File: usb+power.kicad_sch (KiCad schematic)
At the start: 43 parts, among them J1 USB_C_Receptacle_USB2.0_16P, U1 SRV05-4

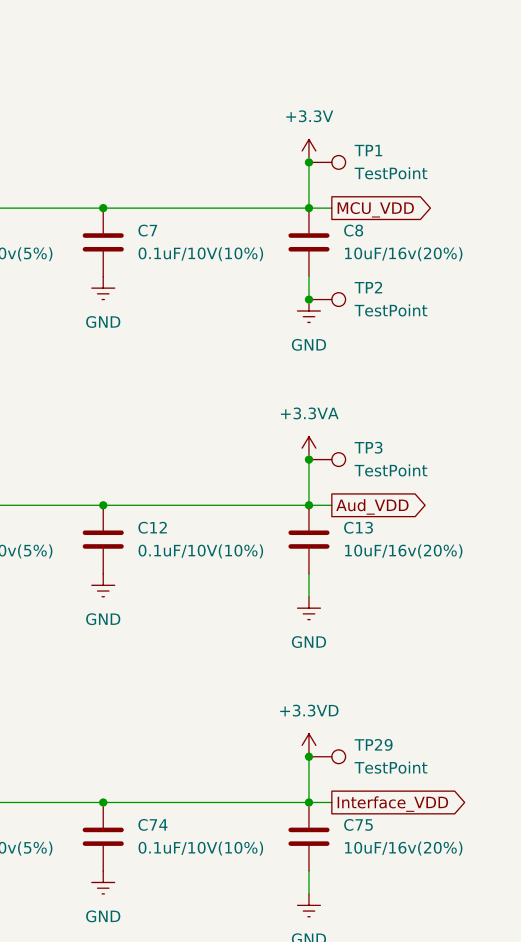
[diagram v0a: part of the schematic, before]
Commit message: Initial population of PCB
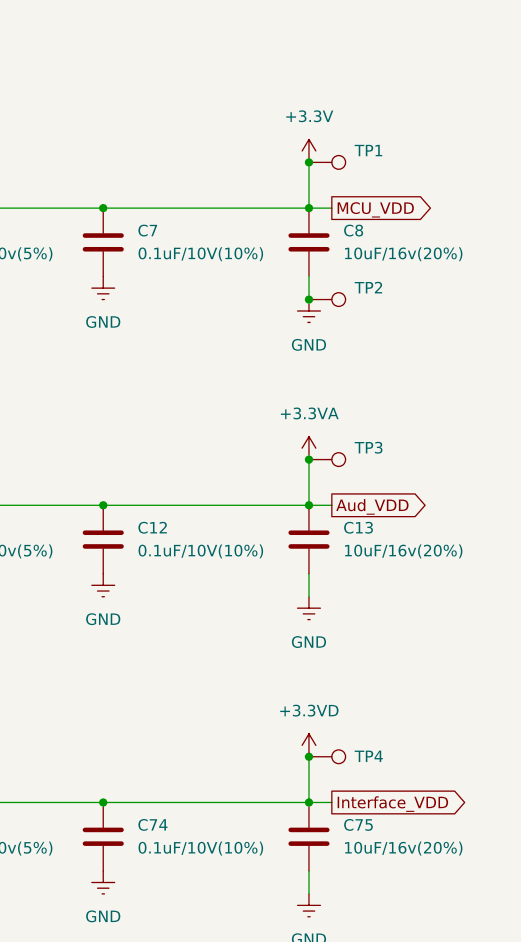
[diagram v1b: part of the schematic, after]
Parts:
- removed TP29: TestPoint, TestPoint:TestPoint_Pad_D1.5mm, symbol Connector:TestPoint
- added TP4: TestPoint, TestPoint:TestPoint_Pad_D1.5mm, symbol Connector:TestPoint
- TP2: footprint (none) -> TestPoint:TestPoint_Pad_D1.5mm
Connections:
- net +3.3VD: now also TP4.1
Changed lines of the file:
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@@
 	)
 	(junction
+		(at 256.54 120.65)
+		(diameter 0)
+		(color 0 0 0 0)
+	)
+	(junction
 		(at 160.02 92.71)
 		(diameter 0)
@@
 	)
 	(junction
-		(at 114.3 125.73)
+		(at 256.54 69.85)
 		(diameter 0)
 		(color 0 0 0 0)
 	)
 	(junction
-		(at 256.54 69.85)
+		(at 114.3 125.73)
 		(diameter 0)
 		(color 0 0 0 0)
@@
 		(color 0 0 0 0)
 	)
-	(junction
-		(at 256.54 120.65)
-		(diameter 0)
-		(color 0 0 0 0)
-	)
 	(no_connect
 		(at 88.9 55.88)
@@
 	)
 	(symbol
-		(lib_id "Diode:SS24")
-		(at 102.87 27.94 180)
+		(lib_id "Connector:TestPoint")
+		(at 256.54 120.65 270)
 		(unit 1)
 		(exclude_from_sim no)
@@
 		(dnp no)
 		(fields_autoplaced yes)
-		(property "Reference" "D1"
-			(at 103.1875 21.59 0)
+		(property "Reference" "TP4"
+			(at 261.62 120.6499 90)
 			(effects
 				(font
 					(size 1.27 1.27)
 				)
+				(justify left)
 			)
 		)
-		(property "Value" "SS24"
-			(at 103.1875 24.13 0)
+		(property "Value" "TestPoint"
+			(at 261.1119 118.11 0)
 			(effects
 				(font
 					(size 1.27 1.27)
 				)
+				(justify right)
+				(hide yes)
 			)
 		)
-		(property "Footprint" "Diode_SMD:D_SMA"
-			(at 102.87 23.495 0)
+		(property "Footprint" "TestPoint:TestPoint_Pad_D1.5mm"
+			(at 256.54 125.73 0)
 			(effects
 				(font
@@
 			)
 		)
-		(property "Datasheet" "https://www.vishay.com/docs/88748/ss22.pdf"
-			(at 102.87 27.94 0)
+		(property "Datasheet" "~"
+			(at 256.54 125.73 0)
 			(effects
 				(font
@@
 			)
 		)
-		(property "Description" "40V 2A Schottky Diode, SMA"
-			(at 102.87 27.94 0)
+		(property "Description" "test point"
+			(at 256.54 120.65 0)
 			(effects
 				(font
@@
 		(pin "1"
 		)
-		(pin "2"
-		)
 		(instances
 			(project "Wave"
 				(path "/d9ae5ab6-a812-4d0b-96e5-05f704754669/5faeef98-962c-45cf-bbaf-2cc942880b89"
-					(reference "D1")
+					(reference "TP4")
 					(unit 1)
 				)
@@
 	)
 	(symbol
-		(lib_id "Connector:TestPoint")
-		(at 256.54 69.85 270)
+		(lib_id "Diode:SS24")
+		(at 102.87 27.94 180)
 		(unit 1)
 		(exclude_from_sim no)
@@
 		(dnp no)
 		(fields_autoplaced yes)
-		(property "Reference" "TP2"
-			(at 261.62 68.5799 90)
+		(property "Reference" "D1"
+			(at 103.1875 21.59 0)
 			(effects
 				(font
 					(size 1.27 1.27)
 				)
-				(justify left)
 			)
 		)
-		(property "Value" "TestPoint"
-			(at 261.62 71.1199 90)
+		(property "Value" "SS24"
+			(at 103.1875 24.13 0)
 			(effects
 				(font
 					(size 1.27 1.27)
 				)
-				(justify left)
 			)
 		)
-		(property "Footprint" ""
-			(at 256.54 74.93 0)
+		(property "Footprint" "Diode_SMD:D_SMA"
+			(at 102.87 23.495 0)
 			(effects
 				(font
@@
 			)
 		)
-		(property "Datasheet" "~"
-			(at 256.54 74.93 0)
+		(property "Datasheet" "https://www.vishay.com/docs/88748/ss22.pdf"
+			(at 102.87 27.94 0)
 			(effects
 				(font
@@
 			)
 		)
-		(property "Description" "test point"
-			(at 256.54 69.85 0)
+		(property "Description" "40V 2A Schottky Diode, SMA"
+			(at 102.87 27.94 0)
 			(effects
 				(font
@@
 		(pin "1"
 		)
+		(pin "2"
+		)
 		(instances
 			(project "Wave"
 				(path "/d9ae5ab6-a812-4d0b-96e5-05f704754669/5faeef98-962c-45cf-bbaf-2cc942880b89"
-					(reference "TP2")
+					(reference "D1")
 					(unit 1)
 				)
@@
 	)
 	(symbol
+		(lib_id "Connector:TestPoint")
+		(at 256.54 69.85 270)
+		(unit 1)
+		(exclude_from_sim no)
+		(in_bom yes)
+		(on_board yes)
+		(dnp no)
+		(fields_autoplaced yes)
+		(property "Reference" "TP2"
+			(at 261.62 68.5799 90)
+			(effects
+				(font
+					(size 1.27 1.27)
+				)
+				(justify left)
+			)
+		)
+		(property "Value" "TestPoint"
+			(at 261.62 71.1199 90)
+			(effects
+				(font
+					(size 1.27 1.27)
+				)
+				(justify left)
+				(hide yes)
+			)
+		)
+		(property "Footprint" "TestPoint:TestPoint_Pad_D1.5mm"
+			(at 256.54 74.93 0)
+			(effects
+				(font
+					(size 1.27 1.27)
+				)
+				(hide yes)
+			)
+		)
+		(property "Datasheet" "~"
+			(at 256.54 74.93 0)
+			(effects
+				(font
+					(size 1.27 1.27)
+				)
+				(hide yes)
+			)
+		)
+		(property "Description" "test point"
+			(at 256.54 69.85 0)
+			(effects
+				(font
+					(size 1.27 1.27)
+				)
+				(hide yes)
+			)
+		)
+		(pin "1"
+		)
+		(instances
+			(project "Wave"
+				(path "/d9ae5ab6-a812-4d0b-96e5-05f704754669/5faeef98-962c-45cf-bbaf-2cc942880b89"
+					(reference "TP2")
+					(unit 1)
+				)
+			)
+		)
+	)
+	(symbol
 		(lib_id "power:Earth")
 		(at 35.56 71.12 0)
@@
 				)
 				(justify left)
+				(hide yes)
 			)
 		)
@@
 				)
 				(justify left)
+				(hide yes)
 			)
 		)
@@
 					(unit 1)
 				)
-			)
-		)
-	)
-	(symbol
-		(lib_id "Connector:TestPoint")
-		(at 256.54 120.65 270)
-		(unit 1)
-		(exclude_from_sim no)
-		(in_bom yes)
-		(on_board yes)
-		(dnp no)
-		(fields_autoplaced yes)
-		(property "Reference" "TP29"
-			(at 261.62 119.3799 90)
-			(effects
-				(font
-					(size 1.27 1.27)
-				)
-				(justify left)
-			)
-		)
-		(property "Value" "TestPoint"
-			(at 261.62 121.9199 90)
-			(effects
-				(font
-					(size 1.27 1.27)
-				)
-				(justify left)
-			)
-		)
-		(property "Footprint" "TestPoint:TestPoint_Pad_D1.5mm"
-			(at 256.54 125.73 0)
-			(effects
-				(font
-					(size 1.27 1.27)
-				)
-				(hide yes)
-			)
-		)
-		(property "Datasheet" "~"
-			(at 256.54 125.73 0)
-			(effects
-				(font
-					(size 1.27 1.27)
-				)
-				(hide yes)
-			)
-		)
-		(property "Description" "test point"
-			(at 256.54 120.65 0)
-			(effects
-				(font
-					(size 1.27 1.27)
-				)
-				(hide yes)
-			)
-		)
-		(pin "1"
-		)
-		(instances
-			(project "Wave"
-				(path "/d9ae5ab6-a812-4d0b-96e5-05f704754669/5faeef98-962c-45cf-bbaf-2cc942880b89"
-					(reference "TP29")
-					(unit 1)
-				)

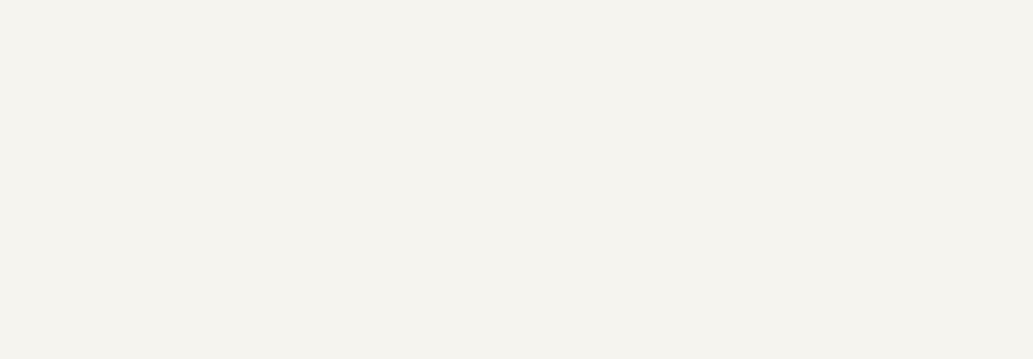
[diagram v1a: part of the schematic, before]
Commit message: Added DSP, Neopixles, MIC's and mounting holes
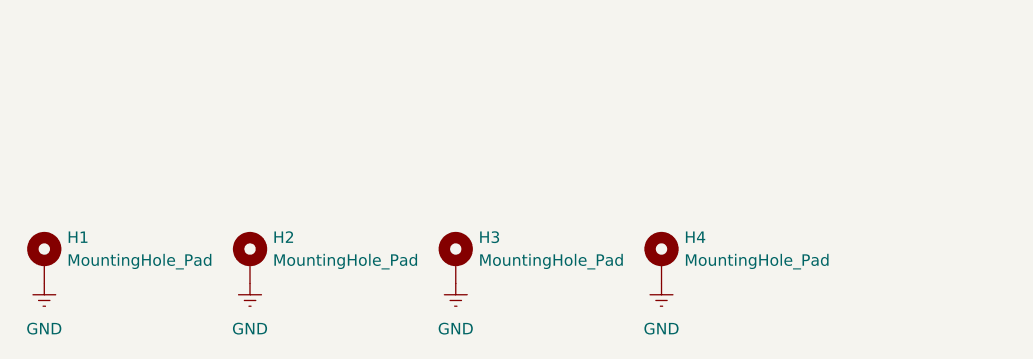
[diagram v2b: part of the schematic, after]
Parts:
- added H1, H2, H3, H4: MountingHole_Pad, MountingHole:MountingHole_3.2mm_M3_Pad_Via, symbol Mechanical:MountingHole_Pad
- C1, C10, C11, C12, C13, C17, C2, C3, C4, C5, C6, C7, C72, C73, C74, C75, C8, C9: footprint Capacitor_SMD:C_0603_1608Metric -> Capacitor_SMD:C_0402_1005Metric
- R1, R2, R3, R4, R5, R6, R7, R76, R77, R78, R8: footprint Resistor_SMD:R_0603_1608Metric -> Resistor_SMD:R_0402_1005Metric
- TP1, TP2, TP3, TP4: footprint TestPoint:TestPoint_Pad_D1.5mm -> TestPoint:TestPoint_Pad_D1.0mm
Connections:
- net GND: now also H1.1, H2.1, H3.1, H4.1
